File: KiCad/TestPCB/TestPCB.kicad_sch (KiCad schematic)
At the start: 42 parts, among them J1 USB_C_Receptacle_PowerOnly_6P, Q5 2N7000, Q6 2N7000, U1 ESP32-S3-WROOM-1, U1 MCP73831-2-OT, U2 TC1185-xCT

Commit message: ADD: all circuits added
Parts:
- added C1, C2: 100nF, Capacitor_SMD:C_0805_2012Metric, symbol Device:C
- added C14, C15, C16, C17, C18, C19: 0.1µF, Capacitor_SMD:C_0805_2012Metric, symbol Device:C
- added CB2: CircuitBreaker_1P, symbol Device:CircuitBreaker_1P
- added D10, D11, D12, D13, D14, D15: WS2812B, LED_SMD:LED_WS2812B_PLCC4_5.0x5.0mm_P3.2mm, symbol LED:WS2812B
- added Q2: Q_Photo_NPN, LED_SMD:LED_0805_2012Metric, symbol Device:Q_Photo_NPN
- added R1, R2, R3: 10kΩ, Resistor_SMD:R_0805_2012Metric, symbol Device:R
- added R7: 330Ω, Resistor_SMD:R_0805_2012Metric, symbol Device:R
- added R_Photo2: 0Ω, Resistor_SMD:R_0805_2012Metric, symbol Device:R
- added SSD2: Conn_01x04_Pin, Connector_PinHeader_2.54mm:PinHeader_1x04_P2.54mm_Vertical_SMD_Pin1Left, symbol Connector:Conn_01x04_Pin
- added TP22, TP24, TP35: SCL, TestPoint:TestPoint_Pad_2.0x2.0mm, symbol Connector:TestPoint
- added TP23, TP25, TP34: SDA, TestPoint:TestPoint_Pad_2.0x2.0mm, symbol Connector:TestPoint
- added TP26: +3.3V, TestPoint:TestPoint_Pad_2.0x2.0mm, symbol Connector:TestPoint
- added TP27, TP28, TP32: GND, TestPoint:TestPoint_Pad_2.0x2.0mm, symbol Connector:TestPoint
- added TP29, TP30: GPIO_Switch, TestPoint:TestPoint_Pad_2.0x2.0mm, symbol Connector:TestPoint
- added TP31, TP37: GPIO_Photo, TestPoint:TestPoint_Pad_2.0x2.0mm, symbol Connector:TestPoint
- added TP33, TP38: GPIO_Pixel, TestPoint:TestPoint_Pad_2.0x2.0mm, symbol Connector:TestPoint
- added TP36: +4.4V, TestPoint:TestPoint_Pad_2.0x2.0mm, symbol Connector:TestPoint
- added U4: LSM6DSM, Package_LGA:LGA-14_3x2.5mm_P0.5mm_LayoutBorder3x4y, symbol Sensor_Motion:LSM6DSM
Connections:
- net at U1.13 (GPIO19/U1RTS/ADC2_CH8/CLK_OUT2/USB_D-): now also R2.1, TP23.1
- net at U1.14 (GPIO20/U1CTS/ADC2_CH9/CLK_OUT1/USB_D+): now also R1.1, TP22.1
- net at U1.19 (GPIO11/TOUCH11/ADC2_CH0/FSPID/FSPIIO5/SUBSPID): now also TP30.1
- net at TP1.1, U1.2 (3V3): now also R1.2, R2.2
- net at U1.5 (GPIO5/TOUCH5/ADC1_CH4): now also TP37.1
- net at U1.6 (GPIO6/TOUCH6/ADC1_CH5): now also TP38.1
- new net: SSD2.1 (Pin_1), TP34.1
- new net: SSD2.2 (Pin_2), TP35.1
- new net: C14.1, D10.1 (VDD), SSD2.3 (Pin_3), TP36.1
- new net: C14.2, D10.3 (VSS), Q2.2 (E), SSD2.4 (Pin_4), TP32.1
- new net: C16.1, D12.1 (VDD)
- new net: C16.2, D12.3 (VSS)
- new net: CB2.1, TP28.1
- new net: C1.2, C2.2, TP27.1, U4.1 (SDO/SA0), U4.2 (SDX), U4.3 (SCX), U4.6 (GND), U4.7 (GND)
- new net: C18.1, D14.1 (VDD)
- new net: C18.2, D14.3 (VSS)
- new net: R7.1, TP33.1
- new net: D10.4 (DIN), R7.2
- new net: C19.1, D15.1 (VDD)
- new net: C19.2, D15.3 (VSS)
- new net: D14.2 (DOUT), D15.4 (DIN)
- new net: C15.1, D11.1 (VDD)
- new net: C15.2, D11.3 (VSS)
- new net: Q2.1 (C), R_Photo2.1
- new net: R3.1, U4.12 (CS)
- new net: C1.1, C2.1, R3.2, TP26.1, U4.5 (VDDIO), U4.8 (VDD)
- new net: TP24.1, U4.13 (SCL)
- new net: CB2.2, TP29.1
- new net: TP25.1, U4.14 (SDA)
- new net: D10.2 (DOUT), D11.4 (DIN)
- new net: C17.1, D13.1 (VDD)
- new net: D13.2 (DOUT), D14.4 (DIN)
- new net: C17.2, D13.3 (VSS)
- new net: D12.2 (DOUT), D13.4 (DIN)
- new net: R_Photo2.2, TP31.1
- new net: D11.2 (DOUT), D12.4 (DIN)
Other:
- note added: "ESP32"
- note added: "FrontPCB"
- note added: "IMU"
- note added: "Switch"
- moved on the sheet: C1, C10, C11, C2, C3, C4, C5, CB1, D1, J1, Q5, Q6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

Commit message: ADD: PCB added
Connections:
- net at C14.1, D10.1 (VDD), SSD2.3 (Pin_3)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: now also C15.1, C16.1, C17.1, C18.1, C19.1, D11.1 (VDD), D12.1 (VDD), D13.1 (VDD), D14.1 (VDD), D15.1 (VDD)
- net at C14.2, D10.3 (VSS), Q2.2 (E)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: now also C15.2, C16.2, C17.2, C18.2, C19.2, D11.3 (VSS), D12.3 (VSS), D13.3 (VSS), D14.3 (VSS), D15.3 (VSS)
- net at TP30.1: now also U1.18 (GPIO10/TOUCH10/ADC1_CH9/FSPICS0/FSPIIO4/SUBSPICS0); no longer U1.19 (GPIO11/TOUCH11/ADC2_CH0/FSPID/FSPIIO5/SUBSPID)
- net at TP38.1: now also U1.24 (GPIO47/SPICLK_P/SUBSPICLK_P_DIFF); no longer U1.6 (GPIO6/TOUCH6/ADC1_CH5)
- net at U1.11 (GPIO18/U1RXD/ADC2_CH7/CLK_OUT3): now also R2.1, TP23.1
- net at U1.21 (GPIO13/TOUCH13/ADC2_CH2/FSPIQ/FSPIIO7/SUBSPIQ): now also TP37.1
- net at U1.5 (GPIO5/TOUCH5/ADC1_CH4): no longer TP37.1
- now unconnected: U1.13 (GPIO19/U1RTS/ADC2_CH8/CLK_OUT2/USB_D-)

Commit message: ADD: PCB connections finished
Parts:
- removed CB1, CB2: CircuitBreaker_1P, symbol Device:CircuitBreaker_1P
- removed J1: USB_C_Receptacle_PowerOnly_6P, symbol Connector:USB_C_Receptacle_PowerOnly_6P
- removed Q2: Q_Photo_NPN, LED_SMD:LED_0805_2012Metric, symbol Device:Q_Photo_NPN
- removed Q5, Q6: 2N7000, Package_TO_SOT_THT:TO-92_Inline, symbol Transistor_FET:2N7000
- added J2: USB4135-GF-A, USB4135GFA, symbol USB4135-GF-A:USB4135-GF-A
- added Q1: SFH_3711, SFH3711, symbol SFH_3711:SFH_3711
- added Q2, Q3: 2N7002, SOT96P240X120-3N, symbol 2N7002:2N7002
- added S1: KMR631NGULCLFS, KMR621NG, symbol KMR631NGULCLFS:KMR631NGULCLFS
- added S2: JS202011SCQN, JS202011SCQN, symbol JS202011SCQN:JS202011SCQN
- C1, C2, C3, C4, C5: footprint (none) -> Capacitor_SMD:C_0805_2012Metric
- D1: footprint (none) -> LED_SMD:LED_0805_2012Metric
- R1, R2: footprint (none) -> Resistor_SMD:R_0805_2012Metric
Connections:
- net at C14.2, C15.2, C16.2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: now also R_Photo2.1
- net at TP28.1: now also S1.2
- net at C11.1, R12.1, TP14.1: now also Q2.3 (D)
- net at C10.1, R11.1, TP17.1: now also Q3.3 (D)
- net at TP18.1, TP19.1: now also S2.2
- net at C1.2, C2.2, C3.2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: now also J2.A12, J2.B12, J2.MP1, J2.MP2, J2.MP3, J2.MP4; no longer C1.1, R1.1, U1.4 (V_{DD})
- net at C2.1, C5.1, U1.3 (V_{BAT})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: now also S2.1
- net at TP29.1: now also S1.1
- net at R9.1, TP9.1: now also Q2.2 (S)
- net at R9.2: now also Q3.1 (G)
- net at R10.1, TP10.1: now also Q3.2 (S)
- net at R10.2: now also Q2.1 (G)
- net at R_Photo2.2: now also Q1.1 (E); no longer TP31.1
- new net: C1.1, J2.A9, J2.B9, R1.1, U1.4 (V_{DD})
- new net: Q1.2 (C), TP31.1
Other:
- moved on the sheet: R_Photo2

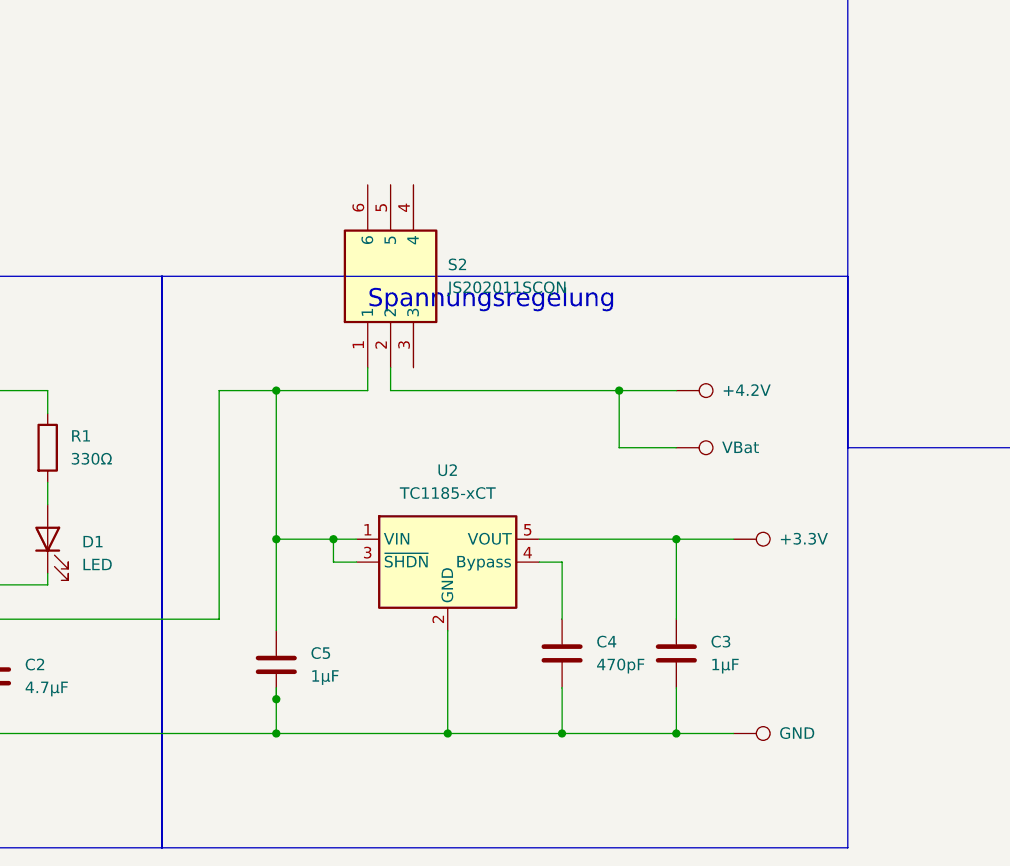
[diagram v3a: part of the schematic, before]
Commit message: ADD: parts arranged in two pcbs
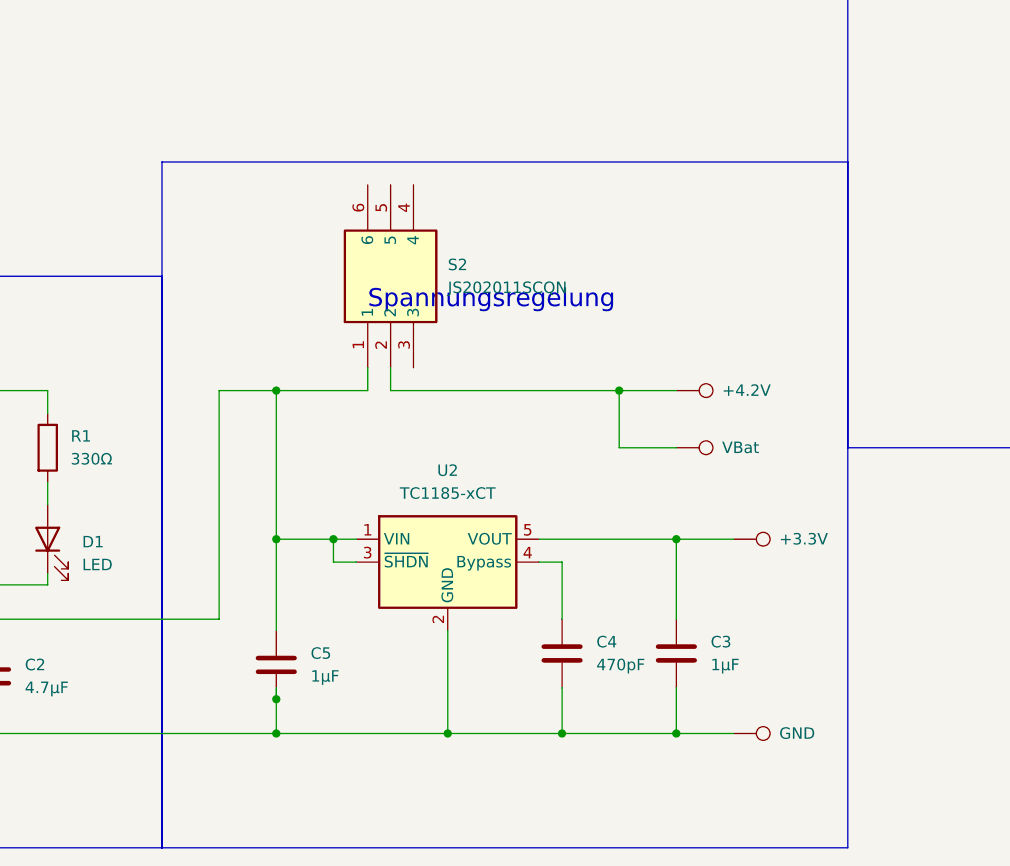
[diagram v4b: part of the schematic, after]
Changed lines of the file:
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@@
     (fill (type none))
   )
-  (rectangle (start 165.1 203.2) (end 241.3 266.7)
+  (rectangle (start 165.1 190.5) (end 241.3 266.7)
     (stroke (width 0) (type default))
     (fill (type none))
